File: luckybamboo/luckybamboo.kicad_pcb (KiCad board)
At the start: 4 copper layers, 70.7 x 53.3 mm, 153 parts, among them J1 NEIGHBOR1, J10 TEST_2P, J11 TEST_2P, J12 TEST_2P, J13 TEST_2P, J14 TEST_2P, J15 TEST_2P, J16 TEST_2P, J17 Conn_Coaxial, J18 Conn_Coaxial, J19 TEST_2P, J2 NEIGHBOR2, J20 TEST_2P, J21 TEST_2P, J22 TEST_2P, J23 TEST_2P, J24 TEST_2P, J25 TEST_2P, J26 TEST_2P, J27 TEST_2P, J28 TEST_2P, J29 TEST_2P, J3 Conn_01x08, J30 TEST_2P, J31 TEST_2P, J32 TEST_2P, J33 TEST_2P, J4 Conn_01x08, J5 Conn_01x08, J6 Conn_01x08, J7 BONUS_ROW, J8 TEST_2P, J9 TEST_2P, U1 ADF7242, U10 ADF7242_balun, U11 ADF7242_balun, U12 HHM2293A1, U13 BGA7H1N6, U14 ADF7242_balun, U15 ADF7242_balun, U16 ADF7242_balun, U17 ADF7242_balun, U2 ADF7242, U3 ADF7242, U4 ADF7242, U5 SKY13322, U6 HHM2293A1, U7 HHM2293A1, U8 ADF7242_balun, U9 ADF7242_balun, X1 XTAL4PIN, X2 XTAL4PIN, X3 XTAL4PIN, X4 XTAL4PIN

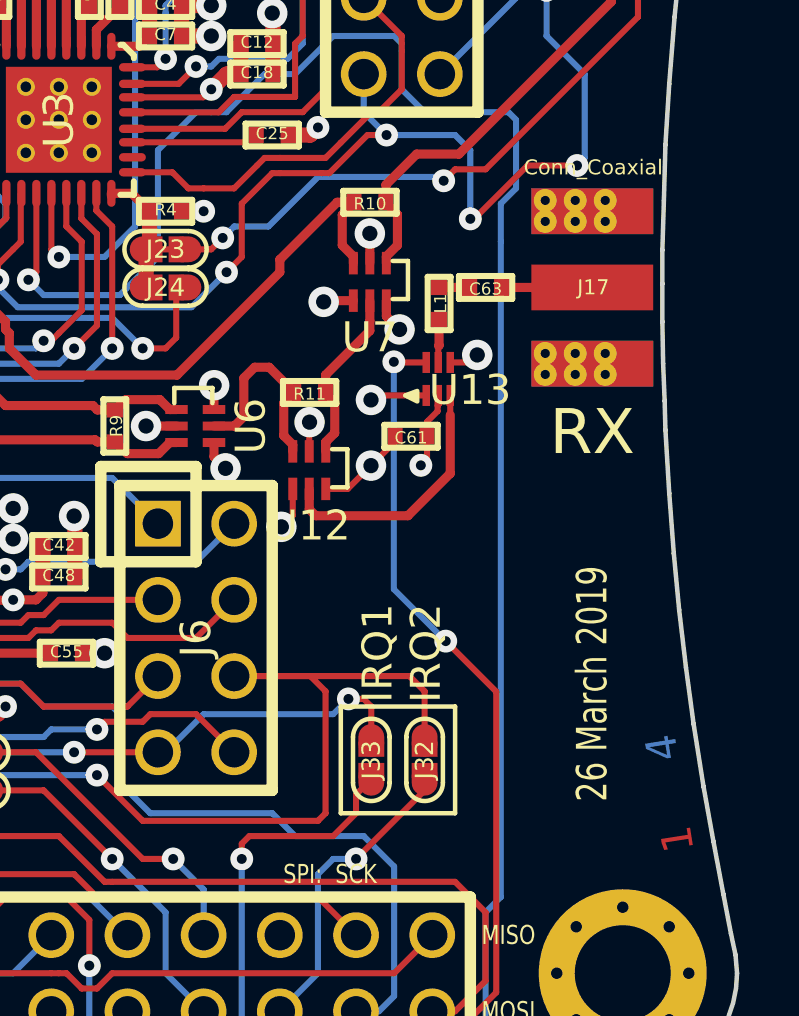
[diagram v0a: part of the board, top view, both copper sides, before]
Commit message: Lucky Bamboo: Fixed sharp routing corner near splitter to U1
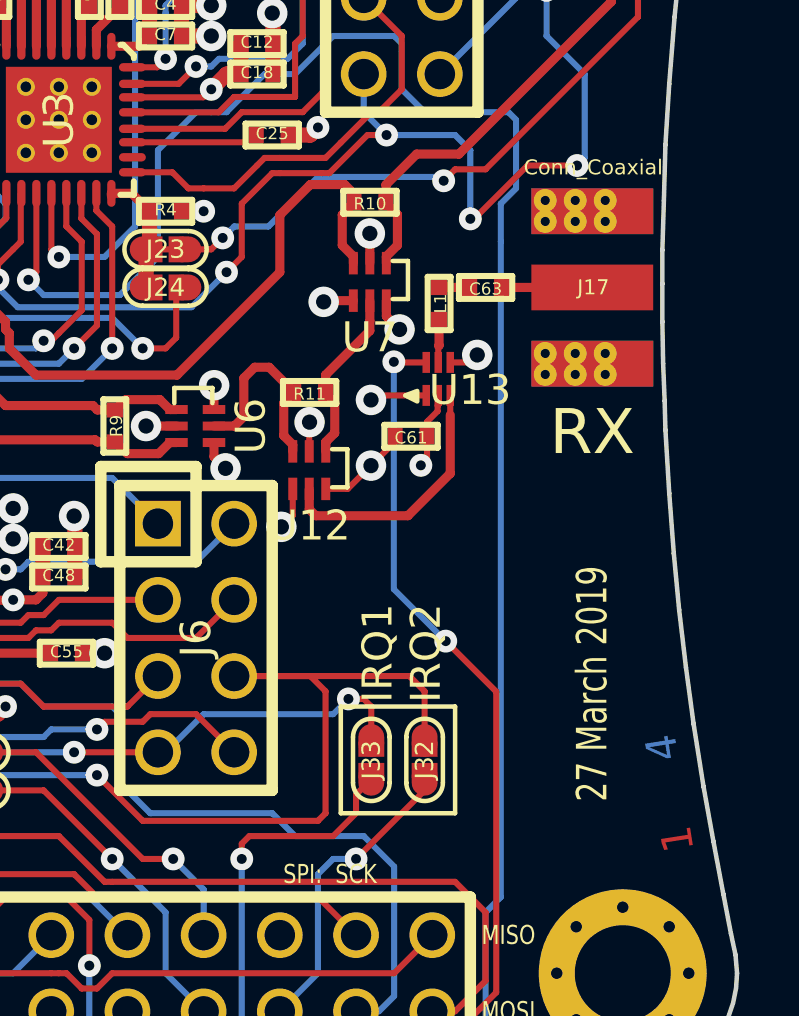
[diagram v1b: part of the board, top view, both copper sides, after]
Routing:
- net /RFIN1: track 55.5 -> 57.1 mm
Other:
- board text added: "27 March 2019"
- board text removed: "26 March 2019"
